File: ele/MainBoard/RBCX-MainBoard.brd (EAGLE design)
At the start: 100 x 100 mm, 261 parts, among them IC1 DRV8833PWP, IC10 INA180A4, IC2 INA180A4, IC3 INA180A4, IC4 DRV8833PWP, IC5 INA180A4, IC6 INA180A4, IC7 INA180A4, IC8 INA180A4, IC9 INA180A4, Q1 CHOOSE_ME, Q3 CHOOSE_ME, Q6 CHOOSE_ME, Q8 CHOOSE_ME, Q9 CHOOSE_ME, U1 STM32F103VCT6, X0 POWER_IN, X1 M3B, X2 M4B, X3 M3B, X4 M4B, X5 POWER_OUT, Y1 3215_2P, Y2 5032/2P

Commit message: MainBoardSCH: Add ESP connectors
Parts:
- removed SJ8: (no value), jumper:SJ_2
- added D11: B5819W, diode:SOD123
- added IM5: STEPDOWN, StepDown:STEPDOWN
- added JP42: ESP_UCOM, pinhead:1X04
- added JP43: ESP_UCOM_AUX, pinhead:1X03
- added JP44: ESP_SPI_AUX1, pinhead:1X03
- added JP45: ESP_SPI2, pinhead:1X06
- added JP46: ESP_SPI_AUX2, pinhead:1X03
- added JP48: ESP_SPI3, pinhead:1X06
- added JP49: ESP_SPI_AUX3, pinhead:1X03
- added JP50, JP56: ESP_I2C_AUX2_5V, pinhead:1X03
- added JP51: ESP_I2C1, pinhead:1X04
- added JP52: ESP_I2C_AUX1, pinhead:1X03
- added JP53: ESP_I2C2, pinhead:1X04
- added JP54: ESP_I2C_AUX2, pinhead:1X03
- added JP55: IM5_EN, pinhead:1X01
- added JP8: ESP_UART_AUX, pinhead:1X03
- added Q2, Q4, Q5, Q7: CHOOSE_ME, transistors:SOT323
- added R105, R106, R109, R110, R113, R114, R117, R118, R119, R120, R121, R97, R98: 180R, rcl_upravena:R0603
- added R107, R115, R116: 4k7, rcl_upravena:R0603
- added R108: 0R, rcl_upravena:R1206S
- added R111, R112: 100k, rcl_upravena:R0603
- added SJ12: (no value), jumper:SJ_2
- JP1: value ESP-I2C-CAN-UART -> ESP_I2C1_5V
- JP2: value ESP_I2C -> ESP_I2C_AUX1_5V; device pinhead:1X04 -> pinhead:1X03
- JP3: value ESP_USART -> ESP_UART; device pinhead:1X07 -> pinhead:1X04
- JP5: value ESP_SPI -> ESP_SPI1
- JP7: value STM_ANALOG -> ESP_I2C2_5V
- R10, R103, R104, R7, R8, R9: value 180R -> 4k7
- R22: value 4k7 -> 180R
- moved R23 1802.1 mm to (-138.4, -1483.4)
- moved R104 1766.7 mm to (-137.2, -1452.9)
- moved JP7 1766.6 mm to (-133.3, -1477.0)
- moved R103 1761.5 mm to (-137.2, -1447.8)
- moved JP1 1756.4 mm to (-133.3, -1459.2)
- moved R8 1746.2 mm to (-137.2, -1442.7)
- moved R7 1733.7 mm to (-137.2, -1437.6)
- moved R96 1713.2 mm to (-137.2, -1404.6)
- moved R95 1688.0 mm to (-137.2, -1384.3)
- moved R94 1682.9 mm to (-137.2, -1379.2)
- moved JP3 1672.6 mm to (-133.3, -1390.7)
- moved JP2 139.0 mm to (-134.6, 435.6)
- moved R9 125.9 mm to (-137.2, 429.3)
- moved R10 121.2 mm to (-135.9, 424.2)
- moved R22 112.1 mm to (-130.8, 424.2)
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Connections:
- net ESP-SPI-!CS renamed ESP-SPI-!CS1
- net ESP_USART_PWR1 renamed ESP_SPI_PWR
- removed net DAC1: IM6.9
- removed net DAC2: IM6.10
- removed net ESP-I2C-SCL-CAN-UART-RX: JP1.3, R7.2
- removed net ESP-I2C-SDA-CAN-UART-TX: JP1.4, R8.2
- removed net ESP-USART-DIR: JP3.5, R96.2
- removed net ESP_I2C_PWR: JP2.1, R22.2, R23.2, SJ8.2
- removed net GPIO0: IM6.7
- removed net I_LED: IM6.23
- removed net N$10: R94.1
- removed net N$12: R95.1
- removed net UART_AUX: IM6.11
- new net ESP-I2C-PWR: JP1.1, JP2.3, JP50.3, JP7.1, R10.2, R103.2, R8.2, SJ11.2
- new net ESP-I2C-SCL-5V: JP1.3, JP7.3, Q2.3, R103.1
- new net ESP-I2C-SDA-5V: JP1.4, JP7.4, Q4.3, R8.1
- new net ESP-SPI-!CS2: JP45.6, R109.2
- new net ESP-SPI-!CS3: JP48.6, R110.2
- new net ESP_BOOT/I_LED: IM6.25, R117.1, R6.1
- new net ESP_UCOM_PWR: JP42.1, SJ12.2
- new net GPIO-1: JP42.3, R97.2
- new net GPIO-2: JP42.4, R98.2
- new net GPIO-3: JP44.1, R106.2
- new net GPIO-4: JP52.1, Q5.2, R22.2, R9.1
- new net GPIO-4-5V: JP2.1, Q5.3, R10.1
- new net GPIO-5: JP43.1, R105.2
- new net GPIO-6: JP8.1, R96.2
- new net GPIO2: IM6.8, R98.1
- new net GPIO3: IM6.9, R106.1
- new net GPIO4: IM6.10, R22.1
- new net GPIO5: IM6.11, R105.1
- new net GPIO6: IM6.26, R96.1
- new net ILED: Q7.2, R115.1, R117.2
- new net ILED-5V: JP56.2, Q7.3, R116.1
- new net ILED_PWR: IM5.OUT, JP56.1, R108.2, R116.2
- new net IM5_EN: IM5.EN, JP55.1
- new net IN3-5V: D11.C, JP50.1
- net +3V3: now also JP43.3, JP44.3, JP45.1, JP46.3, JP48.1, JP49.3, JP51.1, JP52.3, JP53.1, JP54.3, JP8.3, Q2.1, Q4.1, Q5.1, Q7.1, R104.2, R107.1, R111.1, R112.1, R115.2, R23.1, R7.2, R9.2, SJ11.1, SJ12.1; no longer SJ8.1
- net +3V3S: no longer SJ11.1
- net +5V: now also R108.1, SJ12.3; no longer JP1.1, SJ8.3
- net ESP-I2C-SCL: now also JP51.3, JP53.3, Q2.2, R104.1, R113.2; no longer JP2.3, R10.2, R22.1
- net ESP-I2C-SDA: now also JP51.4, JP53.4, Q4.2, R114.2, R7.1; no longer JP2.4, R23.1, R9.2
- net ESP-SPI-MISO: now also JP45.4, JP48.4
- net ESP-SPI-MOSI: now also JP45.3, JP48.3
- net ESP-SPI-SCK: now also JP45.5, JP48.5
- net ESP_BOOT: now also R6.2; no longer IM6.25
- net ESP_COM_RX: now also R118.2
- net ESP_COM_TX: now also R119.2
- net ESP_PROG_RX: now also R120.2
- net ESP_PROG_TX: now also R121.2
- net EXPANDER_RX: now also R119.1
- net EXPANDER_TX: now also R118.1
- net GND: now also IM5.GND, JP42.2, JP43.2, JP44.2, JP45.2, JP46.2, JP48.2, JP49.2, JP50.2, JP51.2, JP52.2, JP53.2, JP54.2, JP56.3, JP8.2
- net GPIO1: now also IM6.7, R97.1; no longer IM6.8
- net I2C_SCL: now also R113.1; no longer R9.1
- net I2C_SDA: now also R114.1; no longer R10.1
- net IN1: now also IM6.3, JP46.1, R112.2; no longer IM6.6
- net IN2: now also IM6.4, JP49.1, R111.2; no longer IM6.5
- net IN3: now also D11.A, IM6.5, R23.2; no longer IM6.4
- net IN4: now also IM6.6, JP54.1, R107.2; no longer IM6.3
- net INTELLIGENT_SERVO: now also IM6.12; no longer IM6.26
- net SPI_!SS1: now also R102.1
- net SPI_!SS2: now also IM6.23, R109.1; no longer IM6.15
- net SPI_!SS3: now also IM6.15, R110.1; no longer IM6.12
- net SPI_SCK: no longer R102.1
- net STM-AIO-POWER: no longer JP7.1, SJ11.2
- net STM-AIO1: no longer JP7.3, R104.2
- net STM-AIO2: no longer JP7.4, R103.2
- net UART2_RX: now also R94.1
- net UART2_TX: now also R95.1
- net UART_RX: now also R121.1
- net UART_TX: now also R120.1
- net VCC: now also IM5.IN

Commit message: MainBoardSCH: Add main voltage regulators and power LEDs
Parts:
- added C13, C14, C24, C47, C48: 220u, rcl_upravena:153CLV-1010
- added C22, C49: 10u, rcl_upravena:C0805
- added C50: 22u, rcl_upravena:B/3528-21R
- added D12, D13, D14, D15, D29: SS34, diode:DO214BA
- added IC11: AMS1117-3.3, v-reg:SOT223
- added IM7: STEPDOWN, StepDown:STEPDOWN
- added JP57: IM7_EN, pinhead:1X01
- added LED6, LED7, LED8: GREEN, led:SML0603
- added R122, R123, R124: 4k7, rcl_upravena:R0603
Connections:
- new net 3V3_IN: C48.+, C49.2, D15.C, D29.C, IC11.3
- new net 5V_IN: C24.+, D12.C, IM7.IN
- new net IM7_EN: IM7.EN, JP57.1
- new net PWRLED_VCC1: LED6.C, R122.2
- new net PWRLED_VCC2: LED7.C, R123.2
- new net PWRLED_VCC3: LED8.C, R124.2
- net +3V3: now also LED8.A
- net +3V3S: now also C50.+, IC11.4, LED7.A
- net +5V: now also C13.+, D13.C, D29.A, IM7.OUT, LED6.A
- net ESP_+5V: now also C14.+, C22.2, D14.C
- net GND: now also C13.-, C14.-, C22.1, C24.-, C47.-, C48.-, C49.1, C50.-, IC11.1, IM7.GND, R122.1, R123.1, R124.1
- net VCC: now also C47.+, D12.A
- net VUSB: now also D13.A, D14.A, D15.A

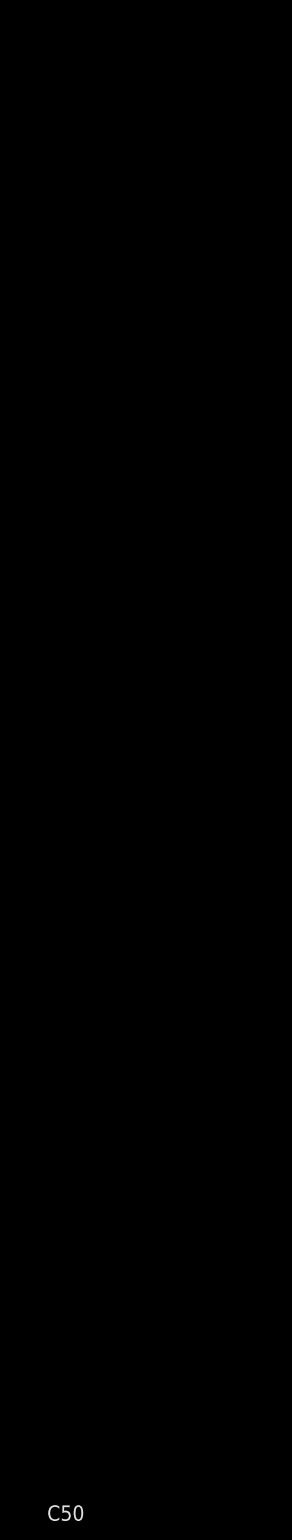
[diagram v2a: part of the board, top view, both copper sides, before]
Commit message: MainBoardSCH: Add bulk capacitor to stepdowns and drivers
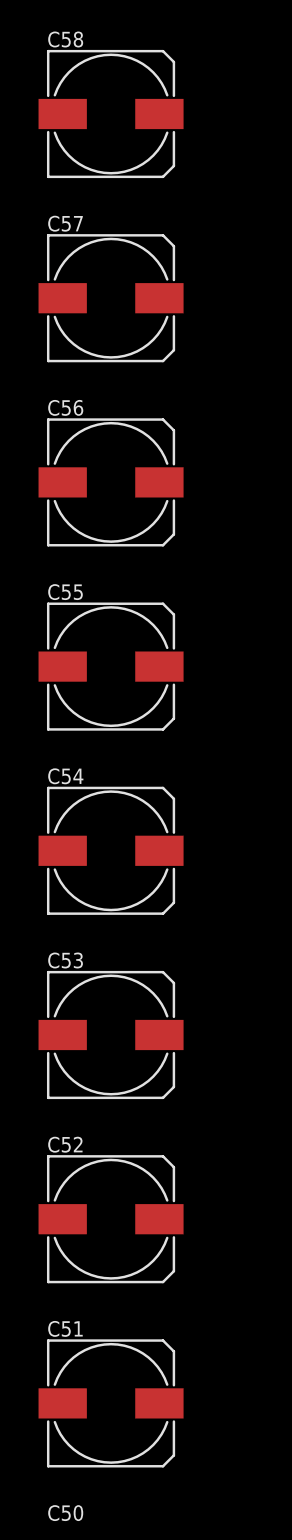
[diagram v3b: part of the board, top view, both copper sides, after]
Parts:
- added C51, C52, C53, C54, C55, C56, C57, C58: 220u, rcl_upravena:153CLV-1010
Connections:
- net GND: now also C51.-, C52.-, C53.-, C54.-, C55.-, C56.-, C57.-, C58.-
- net VCC: now also C51.+, C52.+, C53.+, C54.+, C55.+, C56.+, C57.+, C58.+
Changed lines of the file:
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@@
+<attribute name="VOLTAGE" value="16V" x="-158.75" y="-1521.46" size="1.778" layer="27" display="off"/>
+</element>
+<element name="C51" library="rcl_upravena" package="153CLV-1010" value="220u" x="-144.78" y="725.17" smashed="yes">
+<attribute name="NAME" x="-150.07" y="730.7" size="1.27" layer="25"/>
+<attribute name="VALUE" x="-150.105" y="718.385" size="1.27" layer="27"/>
+<attribute name="VOLTAGE" value="16V" x="-158.75" y="-1521.46" size="1.778" layer="27" display="off"/>
+</element>
+<element name="C52" library="rcl_upravena" package="153CLV-1010" value="220u" x="-144.78" y="740.41" smashed="yes">
+<attribute name="NAME" x="-150.07" y="745.94" size="1.27" layer="25"/>
+<attribute name="VALUE" x="-150.105" y="733.625" size="1.27" layer="27"/>
+<attribute name="VOLTAGE" value="16V" x="-158.75" y="-1521.46" size="1.778" layer="27" display="off"/>
+</element>
+<element name="C53" library="rcl_upravena" package="153CLV-1010" value="220u" x="-144.78" y="755.65" smashed="yes">
+<attribute name="NAME" x="-150.07" y="761.18" size="1.27" layer="25"/>
+<attribute name="VALUE" x="-150.105" y="748.865" size="1.27" layer="27"/>
+<attribute name="VOLTAGE" value="16V" x="-158.75" y="-1521.46" size="1.778" layer="27" display="off"/>
+</element>
+<element name="C54" library="rcl_upravena" package="153CLV-1010" value="220u" x="-144.78" y="770.89" smashed="yes">
+<attribute name="NAME" x="-150.07" y="776.42" size="1.27" layer="25"/>
+<attribute name="VALUE" x="-150.105" y="764.105" size="1.27" layer="27"/>
+<attribute name="VOLTAGE" value="16V" x="-158.75" y="-1521.46" size="1.778" layer="27" display="off"/>
+</element>
+<element name="C55" library="rcl_upravena" package="153CLV-1010" value="220u" x="-144.78" y="786.13" smashed="yes">
+<attribute name="NAME" x="-150.07" y="791.66" size="1.27" layer="25"/>
+<attribute name="VALUE" x="-150.105" y="779.345" size="1.27" layer="27"/>
+<attribute name="VOLTAGE" value="16V" x="-158.75" y="-1521.46" size="1.778" layer="27" display="off"/>
+</element>
+<element name="C56" library="rcl_upravena" package="153CLV-1010" value="220u" x="-144.78" y="801.37" smashed="yes">
+<attribute name="NAME" x="-150.07" y="806.9" size="1.27" layer="25"/>
+<attribute name="VALUE" x="-150.105" y="794.585" size="1.27" layer="27"/>
+<attribute name="VOLTAGE" value="16V" x="-158.75" y="-1521.46" size="1.778" layer="27" display="off"/>
+</element>
+<element name="C57" library="rcl_upravena" package="153CLV-1010" value="220u" x="-144.78" y="816.61" smashed="yes">
+<attribute name="NAME" x="-150.07" y="822.14" size="1.27" layer="25"/>
+<attribute name="VALUE" x="-150.105" y="809.825" size="1.27" layer="27"/>
+<attribute name="VOLTAGE" value="16V" x="-158.75" y="-1521.46" size="1.778" layer="27" display="off"/>
+</element>
+<element name="C58" library="rcl_upravena" package="153CLV-1010" value="220u" x="-144.78" y="831.85" smashed="yes">
+<attribute name="NAME" x="-150.07" y="837.38" size="1.27" layer="25"/>
+<attribute name="VALUE" x="-150.105" y="825.065" size="1.27" layer="27"/>
 <attribute name="VOLTAGE" value="16V" x="-158.75" y="-1521.46" size="1.778" layer="27" display="off"/>
 </element>
@@
 <contactref element="IC11" pad="1"/>
 <contactref element="C50" pad="-"/>
+<contactref element="C51" pad="-"/>
+<contactref element="C52" pad="-"/>
+<contactref element="C53" pad="-"/>
+<contactref element="C54" pad="-"/>
+<contactref element="C55" pad="-"/>
+<contactref element="C56" pad="-"/>
+<contactref element="C57" pad="-"/>
+<contactref element="C58" pad="-"/>
 <wire x1="-134.62" y1="392.43" x2="-134.62" y2="384.81" width="0" layer="19" extent="1-1"/>
 <wire x1="-134.62" y1="372.11" x2="-134.62" y2="384.81" width="0" layer="19" extent="1-1"/>
@@
 <wire x1="-150.96" y1="698.5" x2="-148.78" y2="687.07" width="0" layer="19" extent="1-1"/>
 <wire x1="-146.305" y1="709.93" x2="-150.96" y2="698.5" width="0" layer="19" extent="1-1"/>
+<wire x1="-148.78" y1="725.17" x2="-146.305" y2="709.93" width="0" layer="19" extent="1-1"/>
+<wire x1="-148.78" y1="740.41" x2="-148.78" y2="725.17" width="0" layer="19" extent="1-1"/>
+<wire x1="-148.78" y1="755.65" x2="-148.78" y2="740.41" width="0" layer="19" extent="1-1"/>
+<wire x1="-148.78" y1="770.89" x2="-148.78" y2="755.65" width="0" layer="19" extent="1-1"/>
+<wire x1="-148.78" y1="786.13" x2="-148.78" y2="770.89" width="0" layer="19" extent="1-1"/>
+<wire x1="-148.78" y1="801.37" x2="-148.78" y2="786.13" width="0" layer="19" extent="1-1"/>
+<wire x1="-148.78" y1="816.61" x2="-148.78" y2="801.37" width="0" layer="19" extent="1-1"/>
+<wire x1="-148.78" y1="831.85" x2="-148.78" y2="816.61" width="0" layer="19" extent="1-1"/>
 <wire x1="-137.16" y1="205.22" x2="-134.62" y2="289.56" width="0" layer="19" extent="1-1"/>
 <wire x1="-137.16" y1="193.79" x2="-137.16" y2="205.22" width="0" layer="19" extent="1-1"/>
@@
 <contactref element="D12" pad="A"/>
 <contactref element="C47" pad="+"/>
+<contactref element="C51" pad="+"/>
+<contactref element="C52" pad="+"/>
+<contactref element="C53" pad="+"/>
+<contactref element="C54" pad="+"/>
+<contactref element="C55" pad="+"/>
+<contactref element="C56" pad="+"/>
+<contactref element="C57" pad="+"/>
+<contactref element="C58" pad="+"/>
 <wire x1="-137.65" y1="572.77" x2="-133.16" y2="637.54" width="0" layer="19" extent="1-1"/>
 <wire x1="-137.16" y1="497.84" x2="-137.65" y2="572.77" width="0" layer="19" extent="1-1"/>
+<wire x1="-140.78" y1="725.17" x2="-133.16" y2="637.54" width="0" layer="19" extent="1-1"/>
+<wire x1="-140.78" y1="740.41" x2="-140.78" y2="725.17" width="0" layer="19" extent="1-1"/>
+<wire x1="-140.78" y1="755.65" x2="-140.78" y2="740.41" width="0" layer="19" extent="1-1"/>
+<wire x1="-140.78" y1="770.89" x2="-140.78" y2="755.65" width="0" layer="19" extent="1-1"/>
+<wire x1="-140.78" y1="786.13" x2="-140.78" y2="770.89" width="0" layer="19" extent="1-1"/>
+<wire x1="-140.78" y1="801.37" x2="-140.78" y2="786.13" width="0" layer="19" extent="1-1"/>
+<wire x1="-140.78" y1="816.61" x2="-140.78" y2="801.37" width="0" layer="19" extent="1-1"/>
+<wire x1="-140.78" y1="831.85" x2="-140.78" y2="816.61" width="0" layer="19" extent="1-1"/>
 <wire x1="41.148" y1="57.15" x2="-137.16" y2="497.84" width="0" layer="19" extent="1-1"/>
 <wire x1="41.148" y1="55.626" x2="41.148" y2="57.15" width="0" layer="19" extent="1-1"/>

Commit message: MainBoardSCH: Add buzzer
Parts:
- added D30: B5819W, diode:SOD123
- added Q10: CHOOSE_ME, transistors:SOT323
- added R125, R126: 180R, rcl_upravena:R0603
- added U$1: PIEZO, piezo:PIEZO
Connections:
- new net BUZZER-: D30.A, Q10.3, U$1.-
- new net BUZZER_GATE: Q10.1, R125.1, R126.2
- net +5V: now also D30.C, U$1.+
- net BUZZER: now also R126.1
- net GND: now also Q10.2, R125.2
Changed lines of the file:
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@@
 <attribute name="VOLTAGE" value="16V" x="-158.75" y="-1521.46" size="1.778" layer="27" display="off"/>
+</element>
+<element name="U$1" library="piezo" package="PIEZO" value="PIEZO" x="-147.32" y="-1540.51" smashed="yes">
+<attribute name="NAME" x="-147.8788" y="-1538.0462" size="1.27" layer="25" ratio="10" rot="R90"/>
+</element>
+<element name="Q10" library="transistors" package="SOT323" value="CHOOSE_ME" x="-148.59" y="843.28" smashed="yes">
+<attribute name="NAME" x="-150.495" y="844.785" size="1.27" layer="25"/>
+<attribute name="VALUE" x="-150.495" y="840.505" size="1.27" layer="27"/>
+</element>
+<element name="R125" library="rcl_upravena" package="R0603" value="180R" x="-149.86" y="-1544.32" smashed="yes">
+<attribute name="NAME" x="-150.495" y="-1543.685" size="1.27" layer="25"/>
+<attribute name="VALUE" x="-150.495" y="-1546.225" size="1.27" layer="27"/>
+</element>
+<element name="R126" library="rcl_upravena" package="R0603" value="180R" x="-149.86" y="-1549.4" smashed="yes">
+<attribute name="NAME" x="-150.495" y="-1548.765" size="1.27" layer="25"/>
+<attribute name="VALUE" x="-150.495" y="-1551.305" size="1.27" layer="27"/>
+</element>
+<element name="D30" library="diode" package="SOD123" value="B5819W" x="-148.59" y="849.63" smashed="yes">
+<attribute name="DESCRIPTION" value="40V 1A 600mV @ 1A SOD-123 Schottky Barrier Diodes (SBD) RoHS" x="-148.59" y="-1555.75" size="1.778" layer="27" display="off"/>
+<attribute name="EXTENDED" value="NO" x="-148.59" y="-1555.75" size="1.778" layer="27" display="off"/>
+<attribute name="LCSC_ID" value="C305445" x="-148.59" y="-1555.75" size="1.778" layer="27" display="off"/>
+<attribute name="MF" value="Foshan Blue Rocket Elec" x="-148.59" y="-1555.75" size="1.778" layer="27" display="off"/>
+<attribute name="MF_ID" value="B5819W" x="-148.59" y="-1555.75" size="1.778" layer="27" display="off"/>
+<attribute name="NAME" x="-149.69" y="850.63" size="1.27" layer="25"/>
+<attribute name="PACKAGE" value="SOD-123" x="-148.59" y="-1555.75" size="1.778" layer="27" display="off"/>
+<attribute name="PADS" value="2" x="-148.59" y="-1555.75" size="1.778" layer="27" display="off"/>
+<attribute name="PRICE_100PLUS" value="$0.0176" x="-148.59" y="-1555.75" size="1.778" layer="27" display="off"/>
+<attribute name="PRICE_1PLUS" value="$0.0342" x="-148.59" y="-1555.75" size="1.778" layer="27" display="off"/>
+<attribute name="PRICE_DATE" value="17.03.2020" x="-148.59" y="-1555.75" size="1.778" layer="27" display="off"/>
+<attribute name="VALUE" x="-149.69" y="847.33" size="1.27" layer="27"/>
 </element>
 </elements>
@@
 <contactref element="C57" pad="-"/>
 <contactref element="C58" pad="-"/>
+<contactref element="Q10" pad="2"/>
+<contactref element="R125" pad="2"/>
 <wire x1="-134.62" y1="392.43" x2="-134.62" y2="384.81" width="0" layer="19" extent="1-1"/>
 <wire x1="-134.62" y1="372.11" x2="-134.62" y2="384.81" width="0" layer="19" extent="1-1"/>
@@
 <wire x1="-148.78" y1="816.61" x2="-148.78" y2="801.37" width="0" layer="19" extent="1-1"/>
 <wire x1="-148.78" y1="831.85" x2="-148.78" y2="816.61" width="0" layer="19" extent="1-1"/>
+<wire x1="-147.94" y1="842.38" x2="-148.78" y2="831.85" width="0" layer="19" extent="1-1"/>
 <wire x1="-137.16" y1="205.22" x2="-134.62" y2="289.56" width="0" layer="19" extent="1-1"/>
 <wire x1="-137.16" y1="193.79" x2="-137.16" y2="205.22" width="0" layer="19" extent="1-1"/>
@@
 <wire x1="-134.62" y1="-1489.71" x2="-134.62" y2="-1477.01" width="0" layer="19" extent="1-1"/>
 <wire x1="-150.89" y1="-1511.91" x2="-134.62" y2="-1489.71" width="0" layer="19" extent="1-1"/>
+<wire x1="-149.01" y1="-1544.32" x2="-150.89" y2="-1511.91" width="0" layer="19" extent="1-1"/>
 </signal>
 <signal name="+3V3">
@@
 <contactref element="LED6" pad="A"/>
 <contactref element="D29" pad="A"/>
+<contactref element="U$1" pad="+"/>
+<contactref element="D30" pad="C"/>
 <wire x1="-97.79" y1="-1035.05" x2="-137.16" y2="-1129.03" width="0" layer="19" extent="1-1"/>
 <wire x1="-80.29" y1="-941.07" x2="-97.79" y2="-1035.05" width="0" layer="19" extent="1-1"/>
@@
 <wire x1="-141.75" y1="-1502.41" x2="-137.16" y2="-1129.03" width="0" layer="19" extent="1-1"/>
 <wire x1="-146.54" y1="-1525.27" x2="-141.75" y2="-1502.41" width="0" layer="19" extent="1-1"/>
+<wire x1="-146.05" y1="-1531.62" x2="-146.54" y2="-1525.27" width="0" layer="19" extent="1-1"/>
 <wire x1="-21.336" y1="-325.12" x2="-49.276" y2="-783.59" width="0" layer="19" extent="1-1"/>
 <wire x1="-97.79" y1="121.92" x2="-21.336" y2="-325.12" width="0" layer="19" extent="1-1"/>
@@
 <wire x1="-133.16" y1="584.2" x2="-139.7" y2="551.18" width="0" layer="19" extent="1-1"/>
 <wire x1="-140.22" y1="647.7" x2="-133.16" y2="584.2" width="0" layer="19" extent="1-1"/>
+<wire x1="-150.49" y1="849.63" x2="-140.22" y2="647.7" width="0" layer="19" extent="1-1"/>
 </signal>
 <signal name="ISERVO">
@@
 <signal name="BUZZER">
 <contactref element="U1" pad="67"/>
+<contactref element="R126" pad="1"/>
+<wire x1="-82.49" y1="-955.58" x2="-150.71" y2="-1549.4" width="0" layer="19" extent="1-1"/>
 </signal>
 <signal name="DEBUG_TX">
@@
 <wire x1="-140.78" y1="687.07" x2="-148.81" y2="698.5" width="0" layer="19" extent="1-1"/>
 </signal>
+<signal name="BUZZER-">
+<contactref element="U$1" pad="-"/>
+<contactref element="Q10" pad="3"/>
+<contactref element="D30" pad="A"/>
+<wire x1="-148.59" y1="844.18" x2="-146.69" y2="849.63" width="0" layer="19" extent="1-1"/>
+<wire x1="-146.05" y1="-1539.24" x2="-146.69" y2="849.63" width="0" layer="19" extent="1-1"/>
+</signal>
+<signal name="BUZZER_GATE">
+<contactref element="R126" pad="2"/>
+<contactref element="Q10" pad="1"/>
+<contactref element="R125" pad="1"/>
+<wire x1="-149.01" y1="-1549.4" x2="-149.24" y2="842.38" width="0" layer="19" extent="1-1"/>
+<wire x1="-150.71" y1="-1544.32" x2="-149.01" y2="-1549.4" width="0" layer="19" extent="1-1"/>
+</signal>
 </signals>
